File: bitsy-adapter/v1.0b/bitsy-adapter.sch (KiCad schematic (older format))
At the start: 21 parts, among them J1 PMOD1, J2 PMOD2, J3 PMOD3, J4 5V AUX, J5 5V AUX

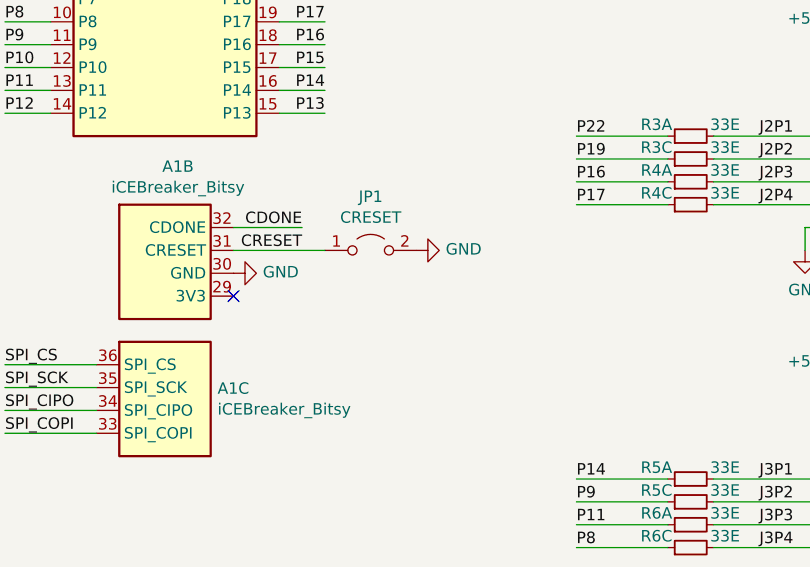
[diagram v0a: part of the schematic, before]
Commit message: Bitsy adapter: finish v1.0b
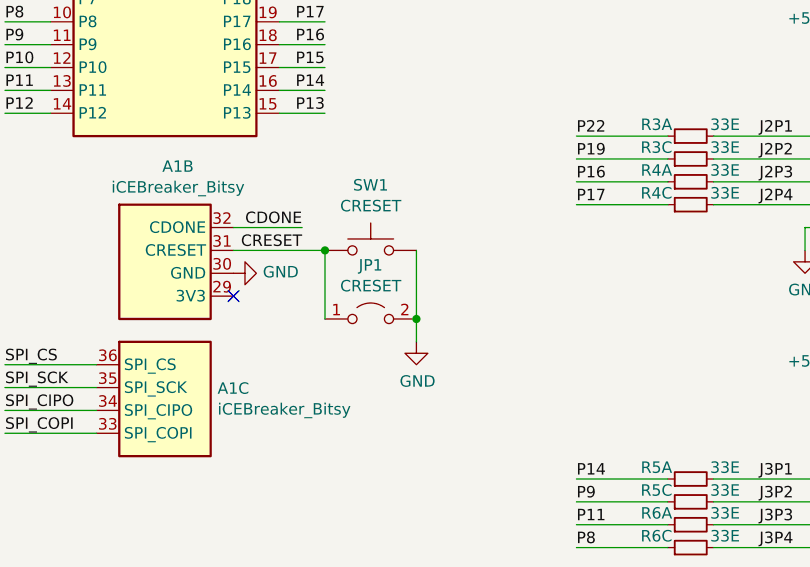
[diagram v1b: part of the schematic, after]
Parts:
- added SW1: CRESET, pkl_buttons_switches:SW_SPST_3x4x2.5, symbol Switch:SW_Push
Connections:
- net CRESET: now also SW1.1
- net GND: now also SW1.2
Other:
- moved on the sheet: JP1
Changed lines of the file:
@@
 Sheet 1 1
 Title "iCEBreaker Bitsy PMOD Adapter"
-Date "2020-11-23"
+Date "2020-12-03"
 Rev "v1.0b"
 Comp "1BitSquared"
@@
 L Jumper:Jumper_2_Open JP1
 U 1 1 5FA94276
-P 6900 4000
-F 0 "JP1" H 6900 4235 50  0000 C CNN
-F 1 "CRESET" H 6900 4144 50  0000 C CNN
-F 2 "Connector_PinHeader_2.54mm:PinHeader_1x02_P2.54mm_Vertical" H 6900 4000 50  0001 C CNN
-F 3 "~" H 6900 4000 50  0001 C CNN
-	1    6900 4000
+P 6900 4300
+F 0 "JP1" H 6900 4535 50  0000 C CNN
+F 1 "CRESET" H 6900 4444 50  0000 C CNN
+F 2 "Connector_PinHeader_2.54mm:PinHeader_1x02_P2.54mm_Vertical" H 6900 4300 50  0001 C CNN
+F 3 "~" H 6900 4300 50  0001 C CNN
+	1    6900 4300
 	1    0    0    -1
 $EndComp
@@
 F 3 "" H 6300 4100 50  0001 C CNN
 	1    6300 4100
-	0    -1   -1   0
-$EndComp
-$Comp
-L power:GND #PWR0123
-U 1 1 5FA693AF
-P 7100 4000
-F 0 "#PWR0123" H 7100 3750 50  0001 C CNN
-F 1 "GND" V 7105 3872 50  0000 R CNN
-F 2 "" H 7100 4000 50  0001 C CNN
-F 3 "" H 7100 4000 50  0001 C CNN
-	1    7100 4000
 	0    -1   -1   0
 $EndComp
@@
 $EndComp
 NoConn ~ 6300 4200
+$Comp
+L Switch:SW_Push SW1
+U 1 1 5FC738FB
+P 6900 4000
+F 0 "SW1" H 6900 4285 50  0000 C CNN
+F 1 "CRESET" H 6900 4194 50  0000 C CNN
+F 2 "pkl_buttons_switches:SW_SPST_3x4x2.5" H 6900 4200 50  0001 C CNN
+F 3 "~" H 6900 4200 50  0001 C CNN
+	1    6900 4000
+	1    0    0    -1
+$EndComp
+Wire Wire Line
+	6700 4300 6700 4000
+Connection ~ 6700 4000
+$Comp
+L power:GND #PWR0121
+U 1 1 5FC7C53C
+P 7100 4400
+F 0 "#PWR0121" H 7100 4150 50  0001 C CNN
+F 1 "GND" H 7105 4227 50  0000 C CNN
+F 2 "" H 7100 4400 50  0001 C CNN
+F 3 "" H 7100 4400 50  0001 C CNN
+	1    7100 4400
+	1    0    0    -1
+$EndComp
+Wire Wire Line
+	7100 4300 7100 4000
+Connection ~ 7100 4300
+Wire Wire Line
+	7100 4400 7100 4300
 $EndSCHEMATC
